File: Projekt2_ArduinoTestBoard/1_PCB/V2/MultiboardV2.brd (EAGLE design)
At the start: 74 x 73.7 mm, 67 parts, among them IC1 MC33269ST-5.0T3, IC2 MC33269D-5.0, Q1 16MHz, Q2 16MHz, T1 FDN304V, U1 LM358D, U2 LP2985-33DBVR, U3 ATMEGA8U2-MU, X1 DC21MMX, Y1 16MHz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

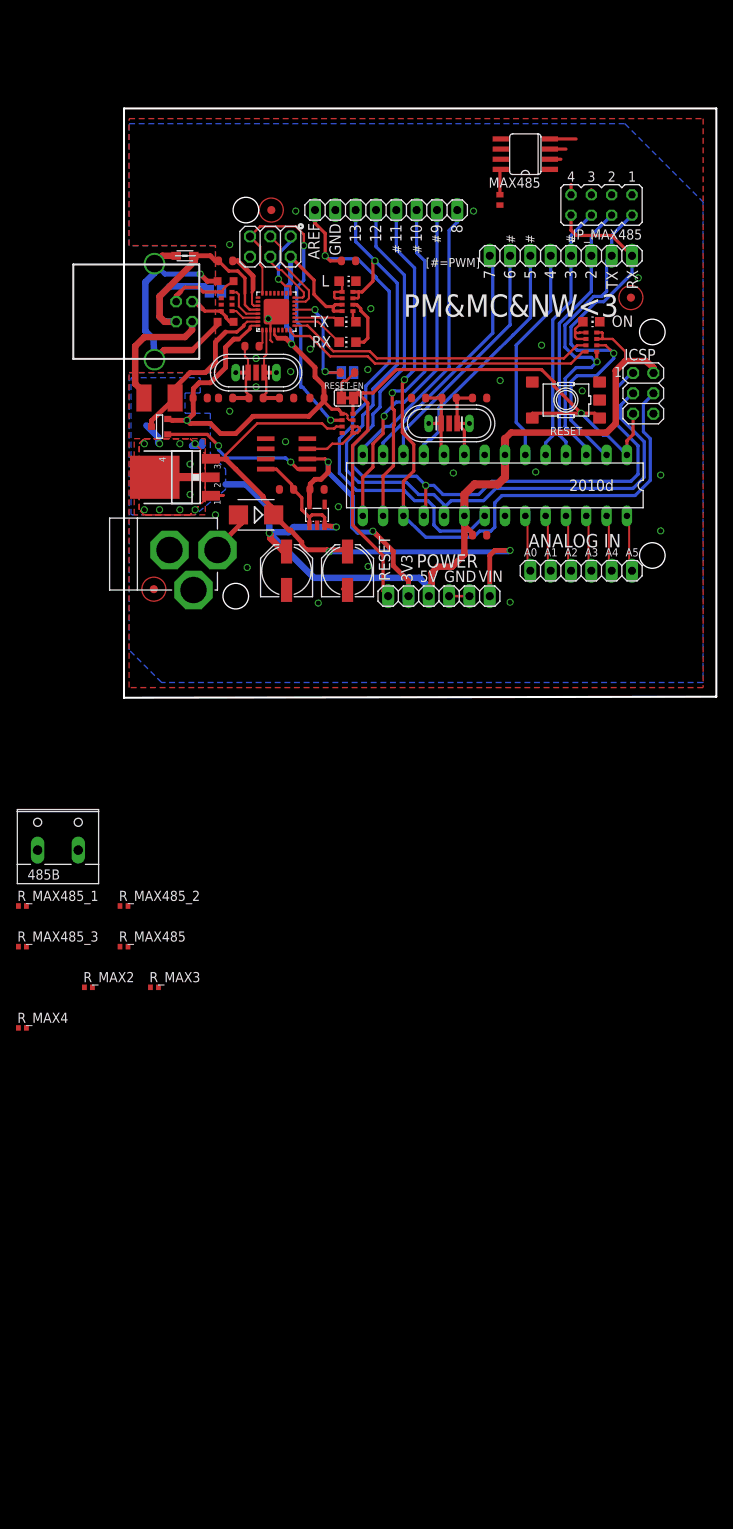
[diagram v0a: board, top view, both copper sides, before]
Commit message: Added SD Card Holder
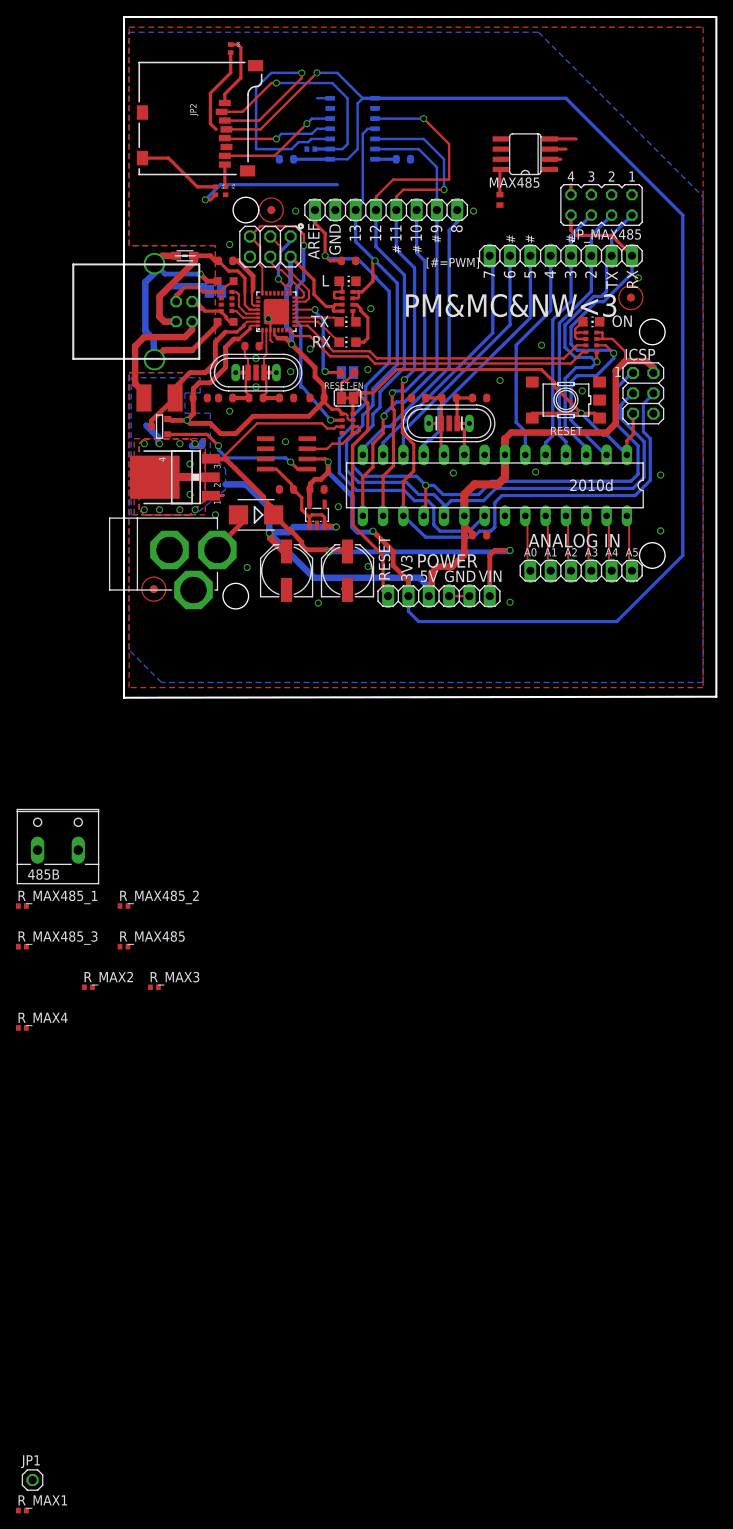
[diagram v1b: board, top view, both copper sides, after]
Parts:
- added C13, C14: 100n, SmartPrj:C0603-ROUND
- added JP1: (no value), pinhead:1X01
- added JP2: USD_CONNECTOR, SparkFun-Connectors:MICRO-SD-SOCKET-PP
- added R4, R5, R6, R7: 100k, rcl:R0402
- added R_MAX1: 10K, rcl:R0402
- added U4: TXB0104, SparkFun-DigitalIC:SO14
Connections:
- new net !CS_3V3: JP2.CS, R7.1, U4.2
- new net CD: JP1.1, JP2.CD2
- new net CDSDSD: JP2.CD1, R6.1
- new net DI_3V3: JP2.DI, U4.3
- new net DO_3V3: JP2.DO, U4.5
- new net RSV@1: JP2.RSV1, R4.1
- new net RSV@2: JP2.RSV2, R5.1
- new net SCK_3V3: JP2.SCLK, U4.4
- net +3V3: now also C14.2, JP2.VCC, R4.2, R5.2, R7.2, U4.1, U4.8
- net +5V: now also C13.2, R6.2, U4.14
- net GND: now also C13.1, C14.1, JP2.GND, JP2.GND1, JP2.GND3, U4.7
- net IO9: now also U4.13
- net MISO: now also U4.10
- net MOSI: now also U4.12
- net SCK: now also U4.11
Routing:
- net +3V3: track 32.4 -> 208.5 mm, vias 2 -> 3
- net DI_3V3: track 0.00 -> 36.4 mm, vias 0 -> 1
- net !CS_3V3: track 0.00 -> 28.3 mm, vias 0 -> 1
- net MISO: track 93.6 -> 120.3 mm, vias 1 -> 2
- net +5V: track 217.3 -> 238.8 mm, vias 14 -> 15
- net MOSI: track 89.3 -> 110.8 mm, vias 1 -> 2
- net DO_3V3: track 0.00 -> 15.1 mm, vias 0 -> 1
- net IO9: track 42.7 -> 56.7 mm
- net SCK_3V3: track 0.00 -> 13.7 mm, vias 0 -> 1
- net SCK: track 99.7 -> 111.4 mm
- net CDSDSD: track 0.00 -> 10.6 mm
- net RSV@1: track 0.00 -> 9.18 mm
- net RSV@2: track 0.00 -> 2.82 mm
- net GND: track 11.8 -> 13.5 mm
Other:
- board size 74 x 73.7 mm -> 74 x 85.1 mm
